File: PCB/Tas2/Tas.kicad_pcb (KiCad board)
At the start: 2 copper layers, 14 x 28 mm, 25 parts, among them J1 Shelly 1, J2 Conn_01x07, J3 USB-C, Q1 PMF170XP,115, Q2 2N7002BKS, U2 LMR16006YDDCR, U3 CH340X

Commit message: Starting new Tas2
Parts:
- removed R8: 4k7, RevK:R_0603
- removed R9: 10k, RevK:R_0603
- removed U3: CH340X, RevK:CH340X
- added C1: 100nF, RevK:C_0603, F.Cu at (176.8, 61.2)
- added R3: 27R, RevK:R_0603, F.Cu at (181.4, 73.0)
- added R4: 27R, RevK:R_0603, F.Cu at (181.4, 74.3)
- added U1: FT231XQ, RevK:QFN-20-1EP_4x4mm_P0.5mm_EP2.5x2.5mm, F.Cu at (180.7, 62.5)
- J2: moved to F.Cu
- Q2: value 2N7002BKS -> PMF250XNEX; footprint RevK:SOT-363_SC-70-6 -> RevK:SOT-323_SC-70
- moved C5 10.9 mm to (172.1, 62.4), turned to 0 degrees
- moved Q2 1.69 mm to (174.0, 59.8), turned to -90 degrees
- moved Q1 0.81 mm to (171.4, 59.8)
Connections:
- net D+ renamed Net-(J3-D+-PadA6)
- net D- renamed Net-(J3-D--PadA7)
- D3 pad 1: RXD -> Net-(D3-K)
- Q1 pad 1: Net-(Q1-G) -> RST
- Q2 pad 1: GND -> RST
- Q2 pad 2: RST -> GND
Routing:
- net RXD: track 48.0 -> 7.46 mm, vias 3 -> 0
- net Net-(D3-K): track 0.00 -> 36.0 mm, vias 0 -> 2
- net TXD: track 29.4 -> 8.13 mm
- net Net-(J3-D--PadA7): track 28.5 -> 9.14 mm, vias 2 -> 0
- net +3V3: track 71.3 -> 53.0 mm
- net D+: track 0.00 -> 18.1 mm, vias 0 -> 2
- net Net-(J3-D+-PadA6): track 28.5 -> 10.4 mm, vias 3 -> 2
- net VBUS: track 14.5 -> 32.4 mm, vias 0 -> 2
- net D-: track 0.00 -> 17.9 mm, vias 0 -> 2
- net GPIO0: track 19.4 -> 3.58 mm, vias 2 -> 0
- net Net-(U1-3V3OUT): track 0.00 -> 15.3 mm, vias 0 -> 2
- net GND: track 100.7 -> 89.4 mm, vias 8 -> 9
- net RST: track 15.5 -> 26.2 mm
- net Net-(J1-Pin_3): track 14.3 -> 6.95 mm
- net Net-(Q1-G): track 4.89 -> 0.00 mm
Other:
- board text added: "FTDI: Invert RTS, CBUS0 mode 9"
- board text removed: "A"

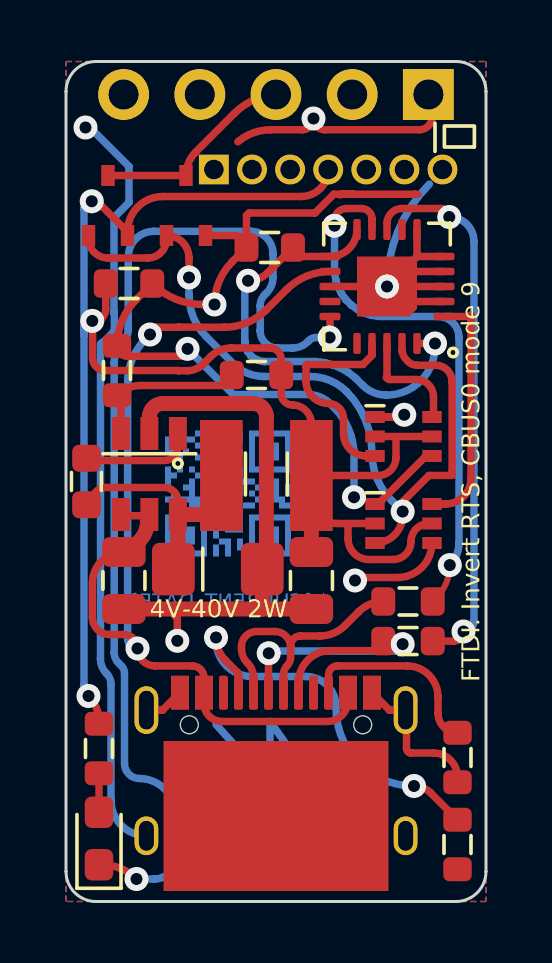
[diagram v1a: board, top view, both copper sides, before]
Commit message: Started on new board using FTDI chip
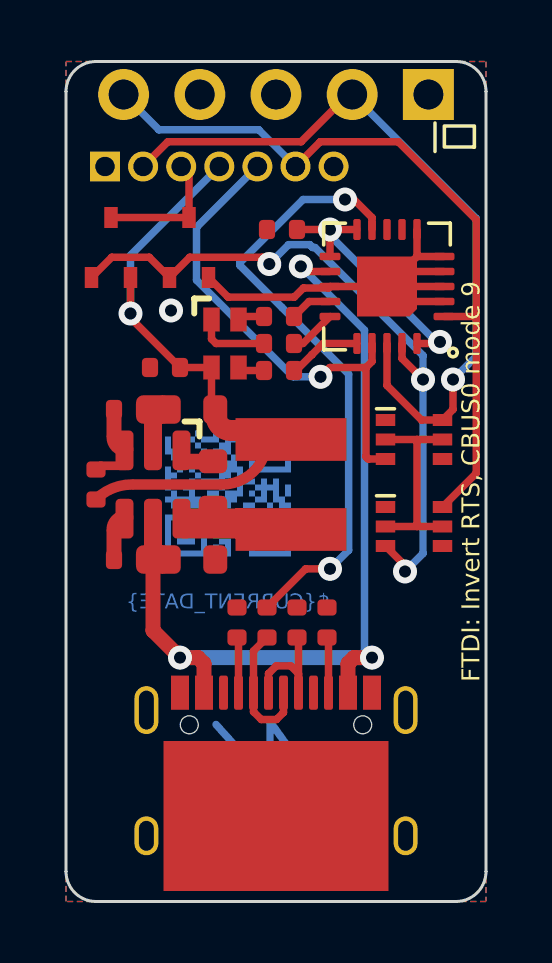
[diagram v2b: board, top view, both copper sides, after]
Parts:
- removed C2: 100nF, RevK:C_0603_
- removed C3: 2.2uF, RevK:C_0805_
- removed C4: 10uF, RevK:C_0805_
- removed D3: LED, LED_SMD:LED_0603_1608Metric_Pad1.05x0.95mm_HandSolder
- removed L1: 6.8uH, RevK:L_4x4_
- removed R5: 680R, RevK:R_0603
- removed U2: LMR16006YDDCR, RevK:SOT-23-Thin-6-Reg
- added C6: 10uF 50V, RevK:C_0603_, F.Cu at (166.0, 62.8)
- added C7: 10uF 6.3V, RevK:C_0603_, F.Cu at (166.0, 64.8)
- added C8: 100nF, RevK:C_0603_, F.Cu at (166.0, 66.7)
- added L2: 10uH, RevK:L_4x4_, F.Cu at (164.6, 71.8)
- added R10: 1M, RevK:R_0402_, F.Cu at (163.3, 66.5)
- added R11: 220R, RevK:R_0402, F.Cu at (177.1, 65.3)
- added R8: 124k, RevK:R_0402_, F.Cu at (163.3, 62.8)
- added R9: 39k2, RevK:R_0402_, F.Cu at (163.3, 64.6)
- added U3: MD8942, RevK:SOT-23-6-MD8942, F.Cu at (172.9, 69.1)
- C1, C5: footprint RevK:C_0603 -> RevK:C_0402
- D4: value Schottky -> RGB; footprint RevK:D_1206_ -> RevK:LED-RGB-1.6x1.6
- R1, R2, R3, R4: footprint RevK:R_0603 -> RevK:R_0402
- R6: value 100k 1% -> 680R; footprint RevK:R_0603 -> RevK:R_0402
- R7: value 30k 1% -> 2K; footprint RevK:R_0603 -> RevK:R_0402
- moved R1 10.4 mm to (175.7, 73.7), turned to 90 degrees
- moved D4 7.52 mm to (175.3, 64.4), turned to -90 degrees
- moved R2 6.26 mm to (178.7, 73.7), turned to -90 degrees
- moved R7 5.69 mm to (177.1, 63.5), turned to 0 degrees
- moved R3 4.75 mm to (176.7, 73.7), turned to 90 degrees
- moved R4 3.75 mm to (177.7, 73.7), turned to 90 degrees
- moved J2 3.63 mm to (175.1, 58.5)
- moved C5 3.05 mm to (173.3, 65.2), turned to 180 degrees
- moved Q1 1.40 mm to (171.5, 61.2)
- moved Q2 1.40 mm to (174.1, 61.2)
- moved R6 1.29 mm to (177.1, 64.4), turned to 0 degrees
- moved C1 0.73 mm to (177.2, 60.6)
- moved D1 0.36 mm to (181.6, 70.5)
- moved D2 0.36 mm to (181.6, 67.6)
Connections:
- R6 pad 1: +3V3 -> Net-(D4-RK)
- R6 pad 2: Net-(U2-FB) -> Net-(U1-CBUS0)
- R7 pad 1: GND -> Net-(D4-GK)
- R7 pad 2: Net-(U2-FB) -> Net-(U1-CBUS1)
- U1 pad 14: unconnected-(U1-CBUS1-Pad14) -> Net-(U1-CBUS1)
- U1 pad 15: Net-(D3-K) -> Net-(U1-CBUS0)
- U1 pad 16: unconnected-(U1-CBUS3-Pad16) -> Net-(U1-CBUS3)
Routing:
- net GND: track 89.4 -> 15.7 mm, vias 9 -> 1
- net Net-(D3-K): track 36.0 -> 0.00 mm, vias 2 -> 0
- net +3V3: track 53.0 -> 19.0 mm, vias 3 -> 1
- net GPIO0: track 3.58 -> 25.4 mm, vias 0 -> 1
- net D+: track 18.1 -> 0.00 mm, vias 2 -> 0
- net TXD: track 8.13 -> 25.3 mm
- net Net-(J3-CC1): track 13.3 -> 1.86 mm, vias 2 -> 0
- net RXD: track 7.46 -> 16.3 mm, vias 0 -> 1
- net Net-(U1-3V3OUT): track 15.3 -> 9.02 mm
- net Net-(J3-D+-PadA6): track 10.4 -> 4.35 mm, vias 2 -> 0
- net Net-(U2-FB): track 5.21 -> 0.00 mm
- net Net-(J3-D--PadA7): track 9.14 -> 4.53 mm
- net Net-(J3-CC2): track 5.90 -> 1.86 mm
- net VBUS: track 32.4 -> 28.8 mm, vias 2 -> 3
- net D-: track 17.9 -> 20.5 mm
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
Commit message: Tracked
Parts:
- moved L2 13.2 mm to (177.5, 69.1), turned to 90 degrees
- moved C6 12.0 mm to (174.2, 71.6), turned to 180 degrees
- moved R10 10.1 mm to (172.1, 71.6), turned to 180 degrees
- moved R8 9.92 mm to (171.0, 69.1), turned to 90 degrees
- moved C8 9.20 mm to (174.9, 69.1), turned to 90 degrees
- moved R9 8.97 mm to (172.1, 66.6)
- moved C7 8.38 mm to (174.2, 66.6), turned to 180 degrees
- moved Art2 0.45 mm to (175.0, 69.6), turned to 90 degrees
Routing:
- net GND: track 15.7 -> 50.3 mm, vias 1 -> 6
- net D+: track 0.00 -> 25.1 mm, vias 0 -> 2
- net RXD: track 16.3 -> 35.9 mm
- net +3V3: track 19.0 -> 32.9 mm
- net TXD: track 25.3 -> 31.4 mm
- net Net-(J1-Pin_3): track 4.41 -> 8.93 mm, vias 0 -> 1
- net D-: track 20.5 -> 22.1 mm
- net GPIO0: track 25.4 -> 24.7 mm
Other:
- board text added: "FTDI: Invert RTS"
- board text removed: "FTDI: Invert RTS, CBUS0 mode 9"

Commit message: Tidy tracks
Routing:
- net Net-(J1-Pin_3): track 8.93 -> 10.9 mm
- net GPIO0: track 24.7 -> 26.6 mm
- net +3V3: track 32.9 -> 32.0 mm
- net RXD: track 35.9 -> 35.1 mm
- net RST: track 24.2 -> 23.7 mm
- net GND: track 50.3 -> 49.9 mm, vias 6 -> 7
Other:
- board text added: "Tasmotiser"
